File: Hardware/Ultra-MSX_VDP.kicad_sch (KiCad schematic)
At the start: 63 parts, among them J3 CBUS, U14 D41464, U15 D41464, U16 D41464, U17 D41464, U3 V9958, U6 LMH1980, Y1 21.477270MHz, Y3 4.433618MHz

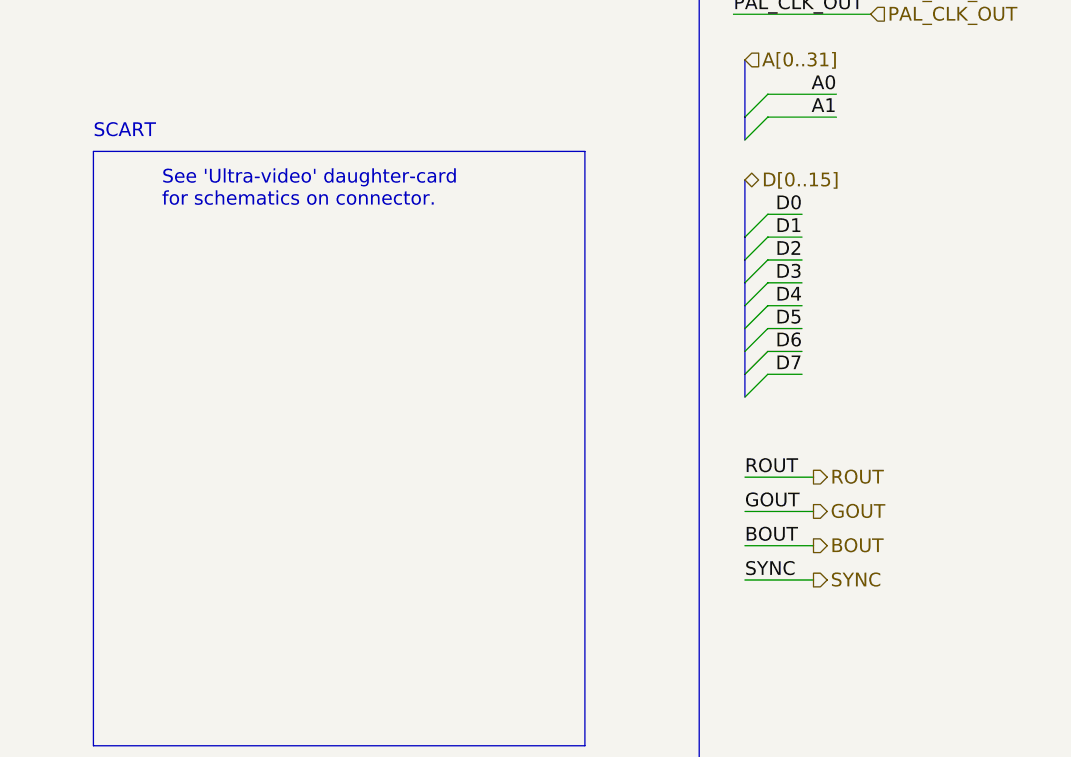
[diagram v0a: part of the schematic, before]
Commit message: Routed the VDP-board further, as well as making it a 4-layer board - also added an exception in the gitignore, for big images.
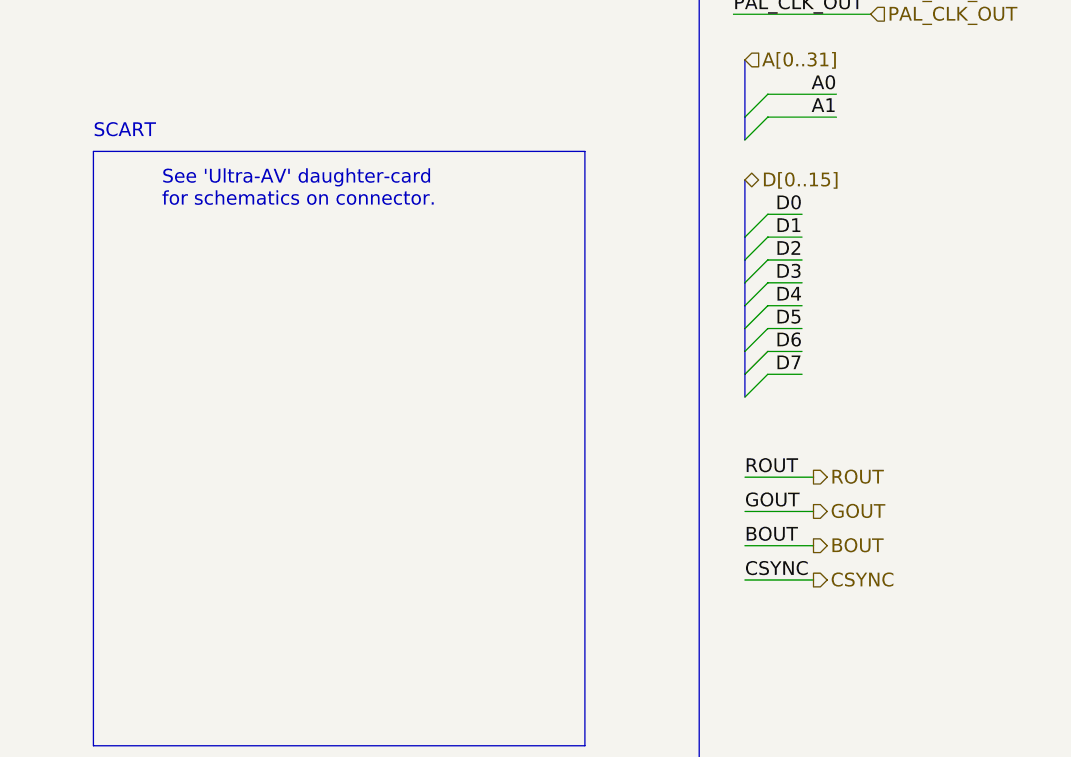
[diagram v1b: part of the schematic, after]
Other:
- note added: "See 'Ultra-AV' daughter-card for schematics on connector."
- note removed: "See 'Ultra-video' daughter-card for schematics on connector."
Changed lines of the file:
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@@
     (effects (font (size 1.524 1.524)) (justify left bottom))
   )
-  (text "See 'Ultra-video' daughter-card \nfor schematics on connector."
+  (text "See 'Ultra-AV' daughter-card \nfor schematics on connector."
     (at 300.99 101.6 0)
     (effects (font (size 1.524 1.524)) (justify left bottom))
@@
     (effects (font (size 1.524 1.524)) (justify left bottom))
   )
-  (label "SYNC" (at 365.76 142.875 0)
+  (label "CSYNC" (at 365.76 142.875 0)
     (effects (font (size 1.524 1.524)) (justify left bottom))
   )
@@
     (effects (font (size 1.524 1.524)) (justify left))
   )
-  (hierarchical_label "SYNC" (shape output) (at 373.38 142.875 0)
-    (effects (font (size 1.524 1.524)) (justify left))
-  )
+  (hierarchical_label "CSYNC" (shape output) (at 373.38 142.875 0)
+    (effects (font (size 1.524 1.524)) (justify left))
+  )

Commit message: Finished the VDP-board, finished up the mixer-section, removed the buffer-pins from the FPGA, and instead added external buffers for the slots, designed a marquee-block with the Ultra-MSX logo, designed the logotype, andmultiple other changes.
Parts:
- removed C1, C5: CTRIM_SGC3S300NM, Capacitor_SMD:C_Trimmer_Sprague-Goodman_SGC3, symbol LRJ-parts:CTRIM_SGC3S300NM
- removed C10, C11, C41, C9: C_CC0805JPX7R9BB104, Capacitor_SMD:C_0805_2012Metric, symbol LRJ-parts:C_CC0805JPX7R9BB104
- removed C12: 47pF, Capacitor_SMD:C_0603_1608Metric, symbol Device:C
- removed C13: 4.7pF, Capacitor_SMD:C_0603_1608Metric, symbol Device:C
- removed C2, C4: 22pF, Capacitor_SMD:C_0603_1608Metric, symbol Device:C
- removed C20: 220uF, Ultra-MSX:Cap_Elec_Radial_10mm, symbol Device:C_Polarized
- removed C3: 0.1uF, Capacitor_SMD:C_0603_1608Metric, symbol Device:C
- removed C6, C7, C8: 330pF, Capacitor_SMD:C_0603_1608Metric, symbol Device:C
- removed J3: CBUS, Connector_PinHeader_2.54mm:PinHeader_1x13_P2.54mm_Vertical_SMD_Pin1Left, symbol LRJ-parts:Conn_GEC13SABN-M30
- removed JP5, JP7: NTSC/PAL, Ultra-MSX:Conn_Pin_Header_3x1_2.54mm, symbol Ultra-MSX:Jumper_NC_Dual
- removed R11: 2.2k, Resistor_SMD:R_0603_1608Metric, symbol Device:R
- removed R13, R14, R15: 75, Resistor_SMD:R_0603_1608Metric, symbol Device:R
- removed R2: 470k, Resistor_SMD:R_0805_2012Metric, symbol Device:R
- removed R20, R21, R22, R23, R25, R49, R50, R51, R52, R53, R54, R55, R56, R57, R58, R59, R60, R9: R_RC0603FR-0710KL, Resistor_SMD:R_0603_1608Metric_Pad0.98x0.95mm_HandSolder, symbol LRJ-parts:R_RC0603FR-0710KL
- removed R27, R5, R6, R61, R7, R8: 100, Resistor_SMD:R_0603_1608Metric, symbol Device:R
- removed R3: 1k, Resistor_SMD:R_0603_1608Metric, symbol Device:R
- removed R4: 1M, Resistor_SMD:R_0805_2012Metric, symbol Device:R
- removed R81, R82, R83, R84: R_CRG0603F470R, Resistor_SMD:R_0603_1608Metric, symbol LRJ-parts:R_CRG0603F470R
- removed U14, U15, U16, U17: D41464, Ultra-MSX:IC_DIP18_300, symbol Ultra-MSX:D41464
- removed U3: V9958, Ultra-MSX:IC_SDIP64_600, symbol Ultra-MSX:V9958
- removed U6: LMH1980, Package_SO:VSSOP-10_3x3mm_P0.5mm, symbol LRJ-parts:LMH1980
- removed Y1: 21.477270MHz, Ultra-MSX:Crystal_HC-49U_Vert, symbol Device:Crystal
- removed Y3: 4.433618MHz, Ultra-MSX:Crystal_HC-49U_Vert, symbol Device:Crystal
- added C17: 220uF, Ultra-MSX:Cap_Elec_Radial_10mm, symbol Device:C_Polarized
- added J3: Ultra-VDP-daughter, Ultra-MSX:Ultra-VDP-daughter, symbol Ultra-MSX:Ultra-VDP-daughter
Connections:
- net +5V: now also J3.16 (Pin_16)
- net A0: now also J3.44
- net A1: now also J3.39
- net BOUT: now also C19.2
- net CLK_VDP: now also J3.13 (Pin_13)
- net CSYNC: now also J3.53
- net D0: now also J3.31
- net D1: now also J3.32
- net D2: now also J3.33
- net D3: now also J3.34
- net D4: now also J3.35
- net D5: now also J3.36
- net D6: now also J3.37
- net D7: now also J3.38
- net GND: now also J3.19 (Pin_19), J3.43, J3.45, J3.52, J3.54, J3.6 (Pin_6), J3.7 (Pin_7), J3.8 (Pin_8)
- net GOUT: now also C18.2; no longer C19.2
- net HSYNC: now also J3.55
- net PALCLK_JPR: now also J3.11 (Pin_11)
- net PAL_CLK_IN: now also J3.40
- net PAL_CLK_OUT: now also J3.17 (Pin_17)
- net ROUT: now also C17.2; no longer C18.2
- net VSYNC: now also J3.56
- net ~{RESET}: now also J3.15 (Pin_15)
- net ~{VDP_INT}: now also J3.20 (Pin_20)
- net ~{VDP_RD}: now also J3.14 (Pin_14)
- net ~{VDP_WAIT}: now also J3.18 (Pin_18)
- net ~{VDP_WR}: now also J3.12 (Pin_12)
- net B-Main: now reaches C19.1
- net B-Main: now also J3.51
- net G-Main: now reaches C18.1
- net G-Main: now also J3.49
- new net A2: J3.27
- new net A3: J3.26
- new net A4: J3.25
- new net A5: J3.24
- new net A6: J3.23
- new net A7: J3.22
- new net A8: J3.21
- new net BLANK: J3.46
- new net D10: J3.41
- new net D11: J3.42
- new net D12: J3.5 (Pin_5)
- new net D13: J3.30
- new net D14: J3.29
- new net D15: J3.28
- new net D8: J3.9 (Pin_9)
- new net D9: J3.10 (Pin_10)
- new net GNDA: J3.47
- new net R-Main: C17.1, J3.50
- new net TCK_VDP: J3.2 (Pin_2)
- new net TDI_VDP: J3.3 (Pin_3)
- new net TDO_VDP: J3.1 (Pin_1)
- new net TMS_VDP: J3.4 (Pin_4)
- new net VREF: J3.48
- no-connect marks 5 -> 0
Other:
- note added: "1.0. Daughter-card containing Video Display Processor"
- note added: "1.1. VDP-card schematic"
- note added: "2. RGB-capacitors (big)"
- note added: "3. SCART"
- note added: "Off-limits names ---- Headers: J1 J2 J3 J4 J5 J6 J7 J11 Chips: U3 U6 U14 Crystals: Y1 Y3 Caps: C1 C2 C3 C9 C10 C11 C12 C13 C14 C15 C16 C73 Resistors: R12 R16 R17"
- note added: "See 'Ultra-VDP' daughter-card project for full schematics."
- note added: "To Mainboard"
- note added: "Ultra-AV daughter-card"
- note removed: "(this leads to RGB-chip)"
- note removed: "1/6 of Crystal Frequency (3,579545 MHz)"
- note removed: "CBUS connector"
- note removed: "PAL Clock Generator"
- note removed: "Processed in the MSX-Engine"
- note removed: "SCART"
- note removed: "To SCART output"
- note removed: "VRAM"

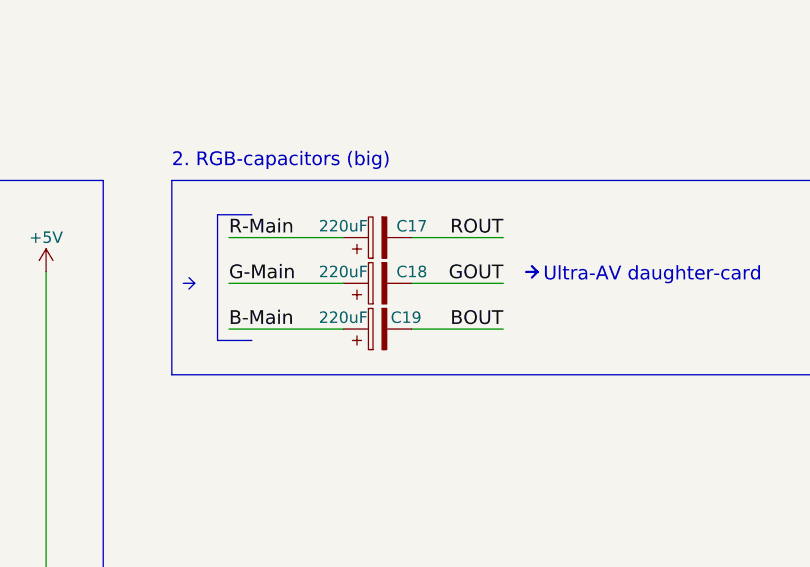
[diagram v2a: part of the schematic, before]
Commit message: Added SD-card slot, made basic 3d-model for sd-card slot, connected it up in the schematic, and numerous other tweaks.
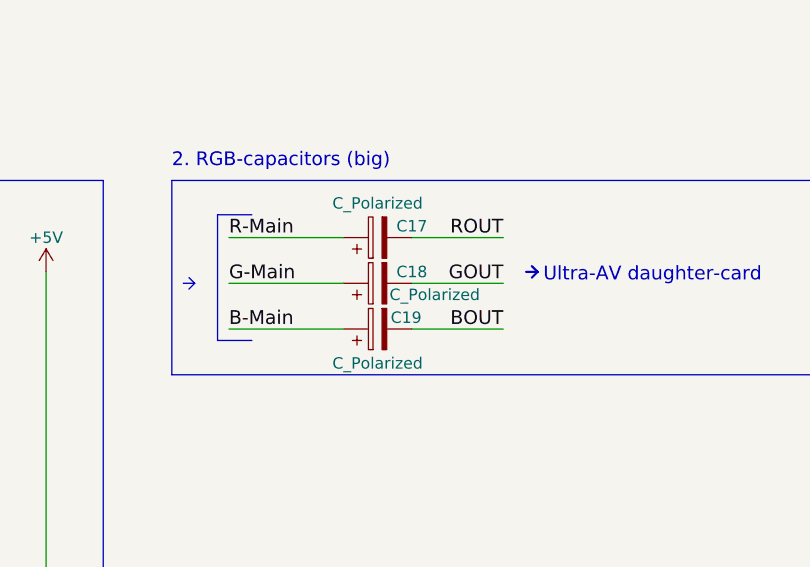
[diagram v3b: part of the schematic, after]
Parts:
- C17, C18, C19: value 220uF -> C_Polarized
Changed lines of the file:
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@@
     (in_bom yes) (on_board yes)
     (property "Reference" "C18" (id 0) (at 128.27 30.48 90))
-    (property "Value" "220uF" (id 1) (at 120.65 30.48 90))
+    (property "Value" "C_Polarized" (id 1) (at 130.81 33.02 90))
     (property "Footprint" "Ultra-MSX:Cap_Elec_Radial_10mm" (id 2) (at 128.27 30.7848 0)
       (effects (font (size 1.27 1.27)) hide)
@@
     (in_bom yes) (on_board yes)
     (property "Reference" "C17" (id 0) (at 128.27 25.4 90))
-    (property "Value" "220uF" (id 1) (at 120.65 25.4 90))
+    (property "Value" "C_Polarized" (id 1) (at 124.46 22.86 90))
     (property "Footprint" "Ultra-MSX:Cap_Elec_Radial_10mm" (id 2) (at 128.27 25.7048 0)
       (effects (font (size 1.27 1.27)) hide)
@@
     (in_bom yes) (on_board yes)
     (property "Reference" "C19" (id 0) (at 127.635 35.56 90))
-    (property "Value" "220uF" (id 1) (at 120.65 35.56 90))
+    (property "Value" "C_Polarized" (id 1) (at 124.46 40.64 90))
     (property "Footprint" "Ultra-MSX:Cap_Elec_Radial_10mm" (id 2) (at 128.27 35.8648 0)
       (effects (font (size 1.27 1.27)) hide)

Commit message: Redesigned VDP-board to include a socket, increased it to 4 layers. Various clean-ups here and there. Improved the printer-port and joystick-port 3D-models. Improved the cooling-fin 3D-model, and added attachment-spring in 3D-model.
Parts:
- added J18: Amphenol_L77HDE15SD1CH4RHNVGA, LRJ:DSUB-Amphenol_L77HDE15SD1CH4RHNVGA, symbol LRJ-parts:Amphenol_L77HDE15SD1CH4RHNVGA
- added J19: Console5_SCART, LRJ:SCART-21_Female_Horizontal_P1.905x2.54mm_EdgePinOffset10.7mm, symbol LRJ-parts:Console5_SCART
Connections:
- net +5V: now also J18.9 (DDC_+5V), J19.8 (SW)
- net GND: now also J18.5 (GND_dig)
- net HSYNC: now also J18.13 (Hor_Sync)
- net VSYNC: now also J18.14 (Ver_Sync)
- net PALCLK_JPR renamed NTSC_CLKO
- net ~{RESET} renamed ~{VDP_RST}
- new net BLUE: J18.3 (BLUE), J19.7 (BLUE)
- new net B_GND: J18.8 (GND_b), J19.5 (BGND)
- new net GREEN: J18.2 (GREEN), J19.11 (GREEN)
- new net G_GND: J18.7 (GND_g), J19.9 (GGND)
- new net RED: J18.1 (RED), J19.15 (RED/CHROMA)
- new net R_GND: J18.6 (GND_r), J19.13 (RGND)
- new net SYNC_GND: J18.10 (Sync_Ret/GND), J19.17 (VGND)
- no-connect marks 0 -> 18
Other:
- note added: "3. SCART output"
- note added: "MON_ID3/NC"
- note added: "Mon_ID0/NC"
- note added: "Mon_ID1/NC"
- note added: "Mon_ID2/NC"
- note added: "VGA clocks: ------------- 640x400 (70Hz) - 25.175 MHz 640x480 (60Hz) - 25.175 MHz Pal clocks: ------------- 704x576 (50Hz) - 4.43361875 MHz NTSC clocks: -------------- 704x480 (60Hz) - 3.579545 MHz"
- note added: "VTO - voltage Controlled Oscillator -------- Frequencies needed: 25.175 MHz 4.43361875 MHz 3.579545 MHz"
- note removed: "3. SCART"
